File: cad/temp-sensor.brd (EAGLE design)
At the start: 70.8 x 40.6 mm, 59 parts, among them Q1 300S14-U, Q2 320S14-U, Q3 320S14-U, U1 SE555D, U2 SE555D, U4 MCP6001UT-I/OT, U6 MCP6001UT-I/OT, U7 MCP6001UT-I/OT, U8 NCV4264-2CST50T3G, U9 ATMEGA328P_TQFP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

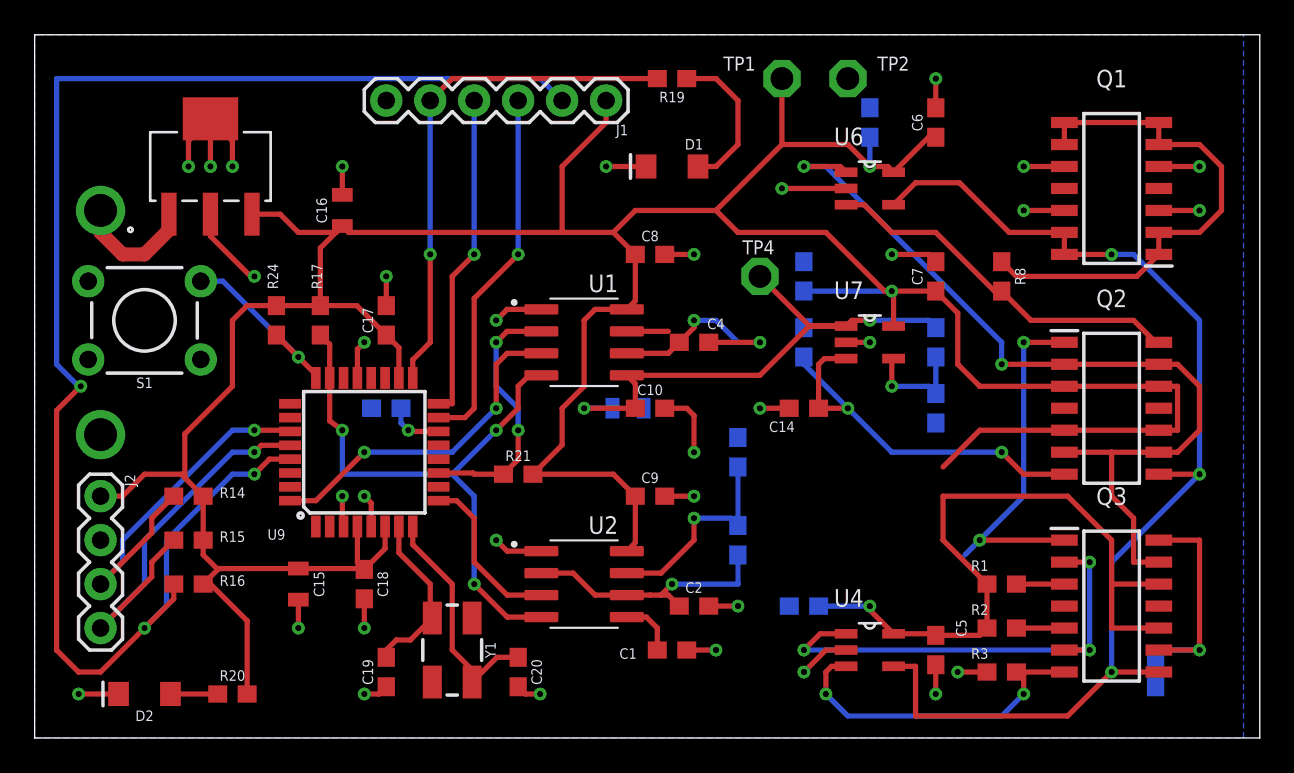
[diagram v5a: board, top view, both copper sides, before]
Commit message: Changes from midterm presentation
Changes from midterm presentation including feeding mono stable timer with bandgap current source and a capacitor. This produces a linear voltage since Ic = C dV/dt.
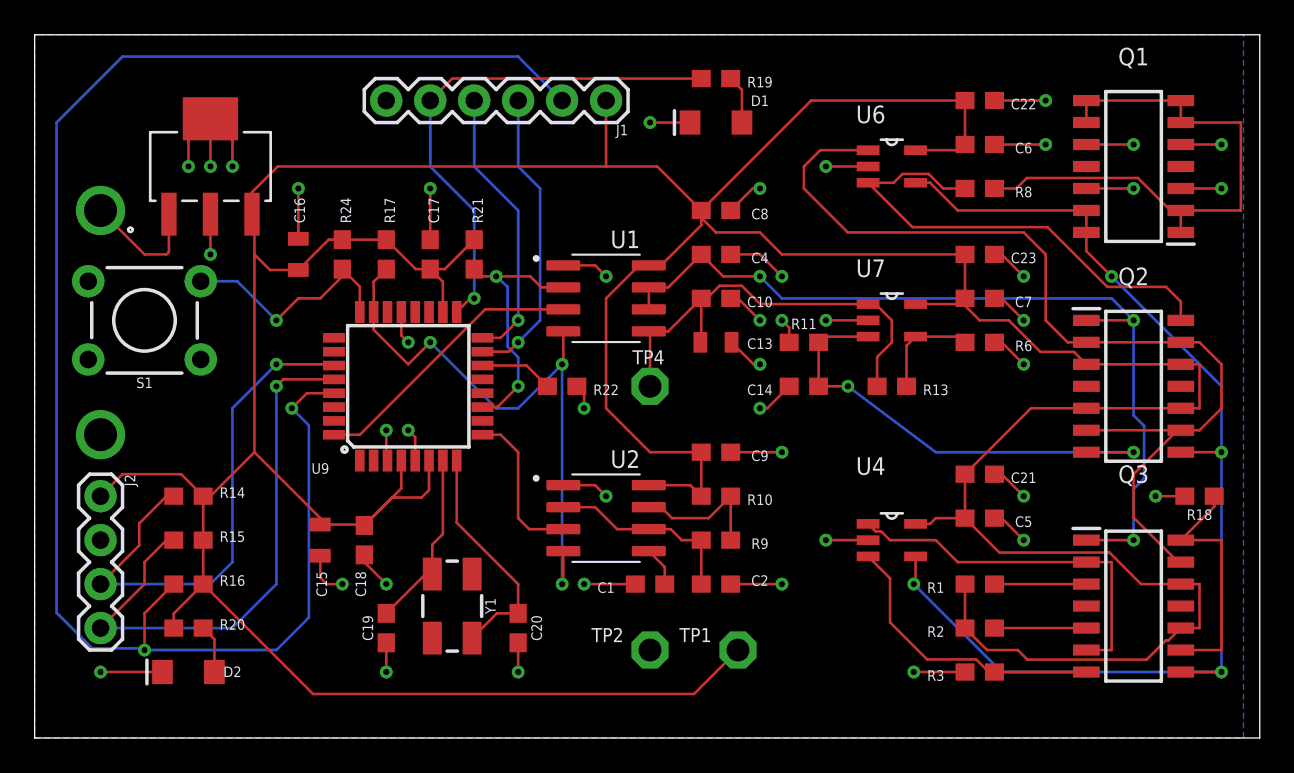
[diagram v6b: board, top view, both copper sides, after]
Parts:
- moved TP2 34.9 mm to (35.6, 5.08)
- moved TP1 33.1 mm to (40.6, 5.08)
- moved R21 13.0 mm to (25.4, 27.9), turned to 90 degrees
- moved C21 12.7 mm to (54.6, 15.2), flipped to the top
- moved R18 10.5 mm to (67.3, 14.0), flipped to the top, turned to 180 degrees
- moved R22 10.2 mm to (30.5, 20.3), flipped to the top
- moved C23 10.2 mm to (54.6, 27.9), flipped to the top, turned to 0 degrees
- moved TP4 8.98 mm to (35.6, 20.3)
- moved C5 8.03 mm to (54.6, 12.7), turned to 0 degrees
- moved C10 7.41 mm to (39.4, 25.4)
- moved C22 6.48 mm to (54.6, 36.8), flipped to the top, turned to 0 degrees
- moved U4 6.48 mm to (49.5, 11.4)
- moved C13 6.35 mm to (39.4, 22.9), flipped to the top, turned to 0 degrees
- moved R17 5.39 mm to (20.3, 27.9)
- moved R24 5.39 mm to (17.8, 27.9)
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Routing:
- net +5V: track 246.0 -> 283.8 mm, vias 3 -> 0
- net GND: track 80.6 -> 106.0 mm, vias 35 -> 43
- net I_BG: track 31.3 -> 50.3 mm
- net SCL: track 23.6 -> 33.2 mm
- net SDA: track 22.2 -> 31.1 mm
- net MCU_RST: track 88.6 -> 96.2 mm, vias 3 -> 2
- net PTAT_IN+: track 21.4 -> 28.2 mm
- net PTAT_BASE: track 50.6 -> 56.9 mm, vias 2 -> 0
- net VPTAT_REF: track 32.2 -> 26.2 mm, vias 2 -> 0
- net N$2: track 8.86 -> 2.81 mm
- net CTAT_BASE: track 27.3 -> 21.5 mm, vias 3 -> 0
- net FREQ_DIS: track 12.0 -> 8.06 mm, vias 1 -> 0
- net FREQ_THRES: track 15.2 -> 11.3 mm, vias 1 -> 0
- net COPI: track 21.1 -> 17.3 mm
- net I_PTAT: track 24.1 -> 27.7 mm
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
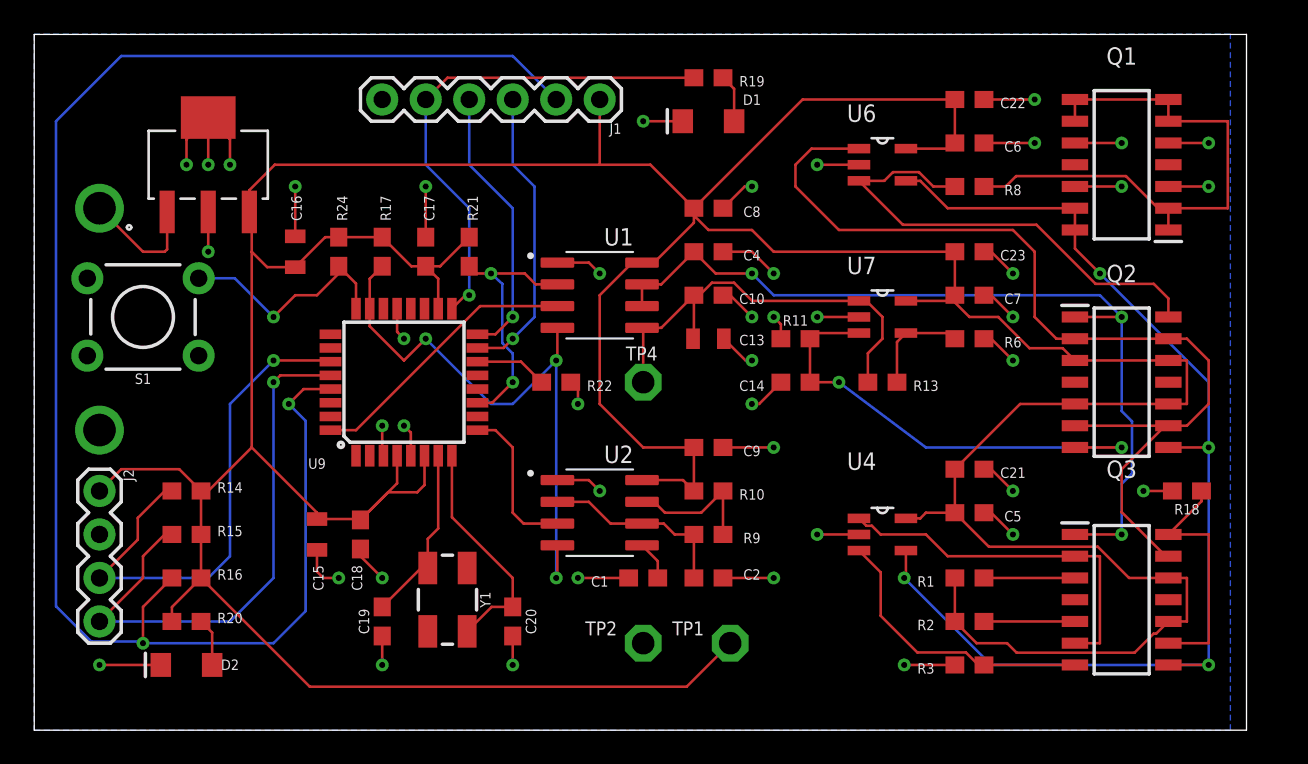
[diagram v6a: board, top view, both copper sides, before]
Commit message: Layout change for exposed copper pad
Removed the vias and routing under Q1, Q2, Q3 matched transistors to make space for a thermally conductive exposed copper pad
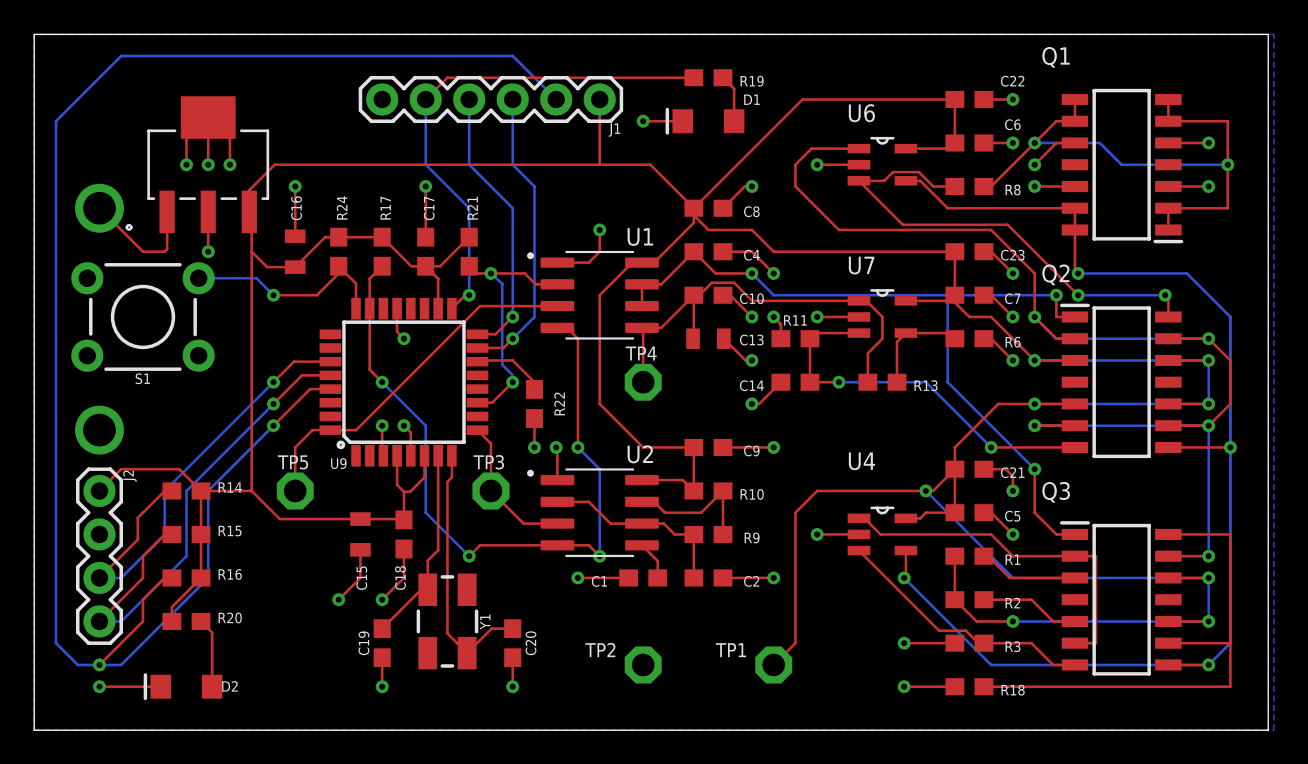
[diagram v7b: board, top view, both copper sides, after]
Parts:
- added TP3, TP5: TPPAD1-13, testpad:P1-13
- moved R18 17.1 mm to (54.6, 2.54)
- moved TP1 2.84 mm to (43.2, 3.81)
- moved C15 2.54 mm to (19.1, 11.4)
- moved C18 2.54 mm to (21.6, 11.4)
- moved R22 1.80 mm to (29.2, 19.1), turned to 90 degrees
- moved R2 1.27 mm to (54.6, 7.62)
- moved Y1 1.27 mm to (24.1, 6.35)
- moved D2 1.27 mm to (8.89, 2.54)
- moved R3 1.27 mm to (54.6, 5.08)
- moved TP2 1.27 mm to (35.6, 3.81)
- moved C19 1.27 mm to (20.3, 5.08)
- moved C20 1.27 mm to (27.9, 5.08)
- moved R1 1.27 mm to (54.6, 10.2)
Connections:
- net FREQ_OUT: now also TP3.TP
- net PULSE_OUT: now also TP5.TP
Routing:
- net START_C: track 14.4 -> 30.5 mm
- net PTAT_BASE: track 56.9 -> 70.9 mm, vias 0 -> 5
- net 555_RST_N: track 35.2 -> 42.5 mm, vias 3 -> 4
- net TEMP_VBE: track 66.7 -> 72.7 mm
- net I_PTAT: track 27.7 -> 22.6 mm
- net PULSE_OUT: track 16.3 -> 21.3 mm
- net +5V: track 283.8 -> 288.7 mm, vias 0 -> 8
- net SCL: track 33.2 -> 28.7 mm
- net SDA: track 31.1 -> 27.3 mm
- net I_BG: track 50.3 -> 47.3 mm
- net XTAL2: track 13.6 -> 15.4 mm
- net GND: track 106.0 -> 107.7 mm
- net CTAT_IN+: track 16.9 -> 15.4 mm
- net 3_NPN_DIODE: track 33.1 -> 34.5 mm, vias 0 -> 2
- net XTAL1: track 10.4 -> 11.7 mm
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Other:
- board size 70.8 x 40.6 mm -> 72.1 x 40.6 mm

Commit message: Add files via upload
Implemented plate extension for temperature reading
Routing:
- net PTAT_IN+: track 28.2 -> 31.7 mm
- net START_C: track 30.5 -> 27.5 mm, vias 0 -> 2
- net CTAT_BASE: track 21.1 -> 23.8 mm, vias 0 -> 2
- net 3_NPN_DIODE: track 34.5 -> 32.9 mm
- net TEMP_VBE: track 72.7 -> 71.9 mm
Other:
- board size 72.1 x 40.6 mm -> 172.5 x 41 mm
- board text added: "T4"
